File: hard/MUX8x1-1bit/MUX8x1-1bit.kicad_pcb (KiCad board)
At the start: 2 copper layers, 129.5 x 39.4 mm, 22 parts, among them J1 Conn_01x01_Male, J10 Conn_01x01_Male, J11 Conn_01x01_Male, J12 Conn_01x03_Male, J13 Conn_01x01_Male, J14 Conn_01x01_Male, J15 Conn_01x01_Male, J16 Conn_01x01_Male, J2 Conn_01x01_Male, J3 Conn_01x01_Male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

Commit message: MUX8x1-1bit v2
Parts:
- moved J1 124.5 mm to (142.2, 56.0)
- moved J8 124.5 mm to (17.8, 56.0)
- moved J2 88.9 mm to (124.5, 56.0)
- moved J7 88.9 mm to (35.6, 56.0)
- moved J3 53.3 mm to (106.7, 56.0)
- moved J6 53.3 mm to (53.3, 56.0)
- moved R2 34.0 mm to (114.3, 45.6), turned to 90 degrees
- moved C2 32.0 mm to (116.8, 41.7), turned to -90 degrees
- moved J14 29.0 mm to (142.3, 49.5), turned to 0 degrees
- moved J11 28.9 mm to (142.2, 34.3), turned to 0 degrees
- moved U2 21.3 mm to (107.3, 41.9), turned to 90 degrees
- moved J4 17.8 mm to (88.9, 56.0)
- moved J5 17.8 mm to (71.1, 56.0)
- moved R1 17.4 mm to (78.1, 44.4), turned to 90 degrees
- moved J13 15.3 mm to (142.3, 47.0)
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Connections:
- net /~E0 renamed /~{E0}
- net /~E1 renamed /~{E1}
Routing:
- net GND: track 169.9 -> 63.3 mm, vias 2 -> 0
- net /~{E0}: track 103.4 -> 32.5 mm, vias 0 -> 2
- net /~{E1}: track 75.4 -> 33.7 mm, vias 1 -> 0
- net /D4: track 50.8 -> 85.1 mm, vias 2 -> 0
- net /S1.2: track 58.8 -> 34.9 mm
- net /S1.1: track 59.4 -> 36.5 mm
- net /S1.0: track 59.9 -> 38.2 mm
- net /D5: track 61.9 -> 82.3 mm, vias 1 -> 0
- net /D6: track 82.6 -> 102.3 mm, vias 1 -> 0
- net /D2: track 53.1 -> 65.3 mm
- net /S0.2: track 81.5 -> 71.9 mm
- net /S0.1: track 82.0 -> 73.6 mm
- net /O0: track 82.4 -> 90.5 mm, vias 0 -> 2
- net /D1: track 71.3 -> 78.7 mm
- net /S0.0: track 82.5 -> 75.2 mm
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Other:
- net class Default removed
- board text added: "25.03.26"
- board text added: "~{E0}"
- board text added: "~{E1}"
- board text removed: "25.06.25"
- board text removed: "~E0"
- board text removed: "~E1"

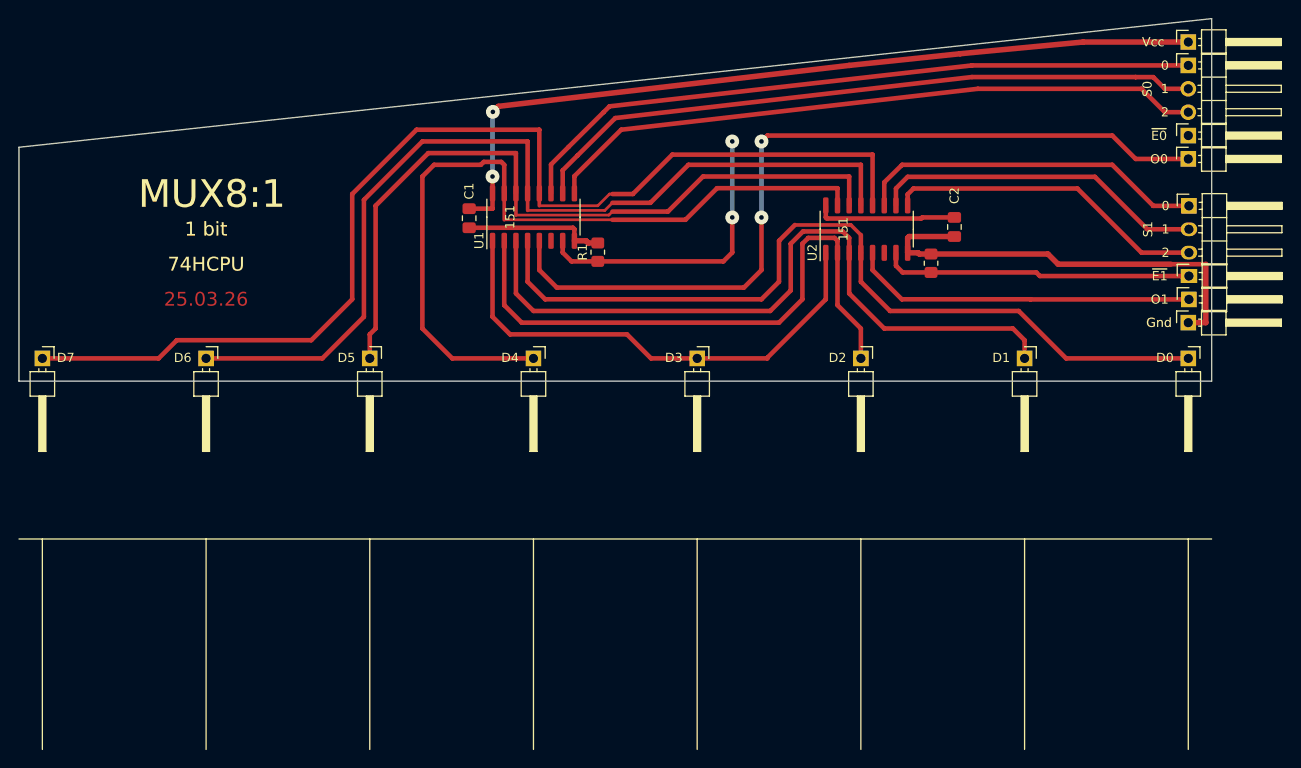
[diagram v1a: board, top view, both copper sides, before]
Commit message: MUX8x1-1bit v2 is finished
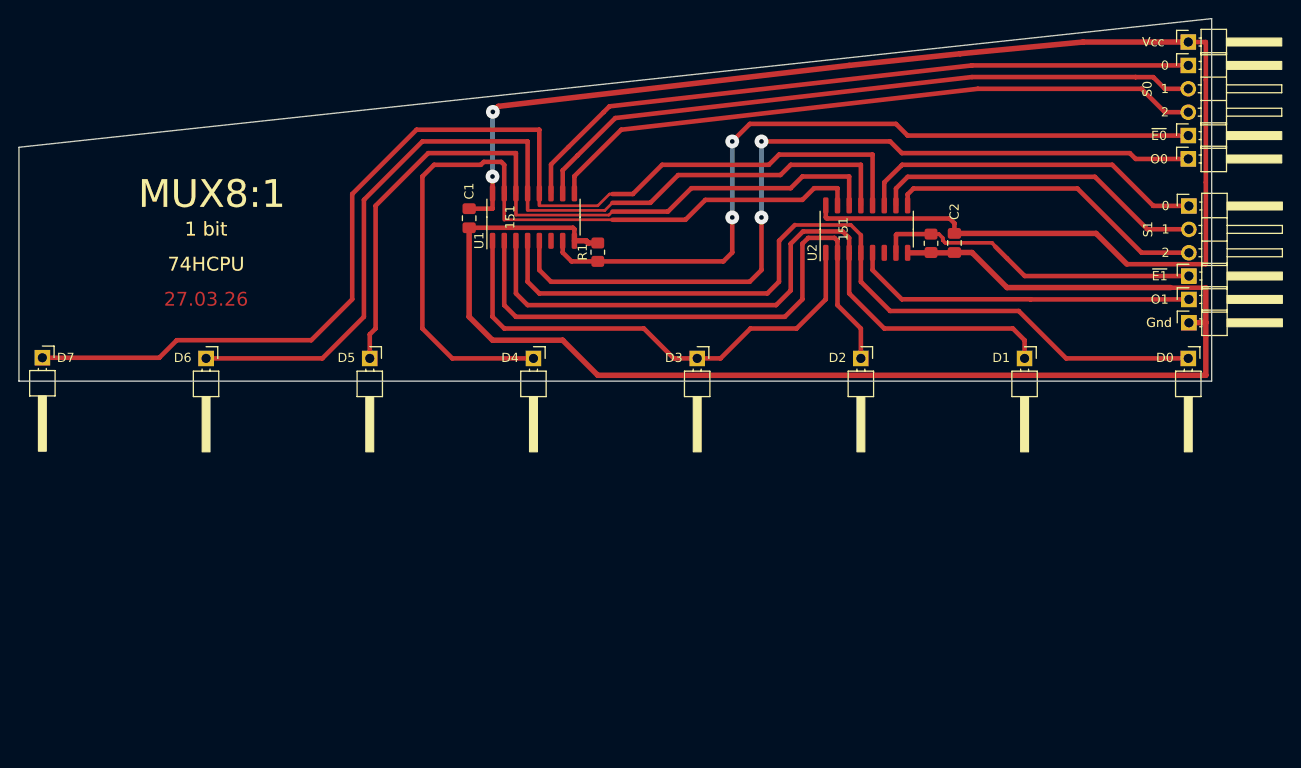
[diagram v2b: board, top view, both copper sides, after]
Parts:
- moved R2 2.16 mm to (114.3, 43.5), turned to -90 degrees
- moved C2 1.73 mm to (116.8, 43.4)
- moved J16 0.07 mm to (142.3, 52.1)
- moved J8 0.07 mm to (17.8, 55.9)
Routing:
- net GND: track 63.3 -> 153.1 mm
- net VCC: track 104.7 -> 160.7 mm
- net /~{E0}: track 32.5 -> 83.4 mm
- net /~{E1}: track 33.7 -> 35.9 mm
- net /O0: track 90.5 -> 89.5 mm
- net /D1: track 78.7 -> 78.2 mm
- net /D2: track 65.3 -> 64.7 mm
- net /D0: track 91.9 -> 91.4 mm
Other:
- board text added: "27.03.26"
- board text removed: "25.03.26"

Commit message: MUX8x1-1bit v2 is almost ready
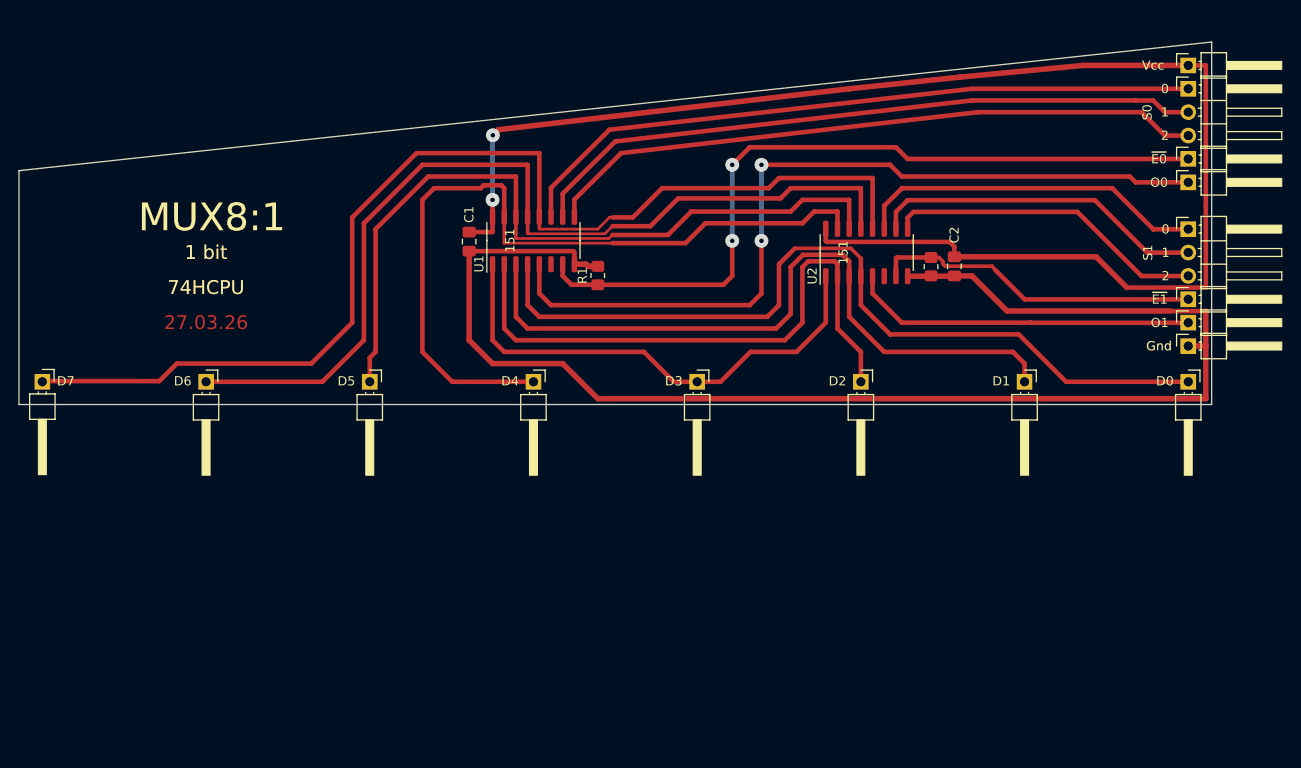
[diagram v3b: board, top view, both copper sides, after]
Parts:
- moved U1 2.54 mm to (71.1, 43.1)
- moved U2 2.54 mm to (107.3, 44.5)
- moved J9 2.54 mm to (142.2, 26.7)
- moved C1 2.54 mm to (64.1, 43.3)
- moved C2 2.54 mm to (116.8, 46.0)
- moved J1 2.54 mm to (142.2, 58.5)
- moved J10 2.54 mm to (142.2, 34.3)
- moved J11 2.54 mm to (142.2, 36.8)
- moved J15 2.54 mm to (142.2, 24.1)
- moved J2 2.54 mm to (124.5, 58.5)
- moved J3 2.54 mm to (106.7, 58.5)
- moved J4 2.54 mm to (88.9, 58.5)
- moved J5 2.54 mm to (71.1, 58.5)
- moved J6 2.54 mm to (53.3, 58.5)
- moved J7 2.54 mm to (35.6, 58.5)
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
